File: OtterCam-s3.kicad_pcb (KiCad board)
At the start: 4 copper layers, 49.7 x 49.7 mm, 167 parts, among them J1 UART, J2 SD, J3 USB, J4 49F-1201GYD2NL, J5 MIPI, Q1 DTA114YKA, SW1 RST, U1 AllWinner-S3(FBGA-234), U2 AXP209(QFN-48), U3 SY8089AAAC, U4 AP6236, X1 26Mhz TCXO, Y1 32.768kHz, Y2 24MHz

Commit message: updated files
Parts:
- J3: footprint otter:USB-C 16Pin -> otter:918-418K2022Y40004
- J4: value 49F-1201GYD2NL -> RJ45_Shielded; footprint otter:49F-1201GYDXNL -> otter:1-338088-3
- moved J4 4.35 mm to (60.8, 68.9), turned to 0 degrees
- moved D5 3.96 mm to (56.0, 90.6)
- moved R19 3.96 mm to (58.5, 90.6)
- moved J3 1.97 mm to (55.9, 85.2)
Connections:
- J4 pad 1: EPHY_RX_P -> Net-(J4-Pad1)
- J4 pad 2: EPHY_RX_N -> Net-(J4-Pad2)
- J4 pad 3: Net-(C67-Pad2) -> Net-(J4-Pad3)
- J4 pad 6: Net-(C66-Pad2) -> Net-(J4-Pad6)
- J4 pad 7: EPHY_TX_P -> Net-(J4-Pad7)
- J4 pad 8: EPHY_TX_N -> Net-(J4-Pad8)
- J4 pad SH: Net-(C65-Pad1) -> GND
- R56 pad 2: Net-(J4-Pad10) -> Net-(R56-Pad2)
- R57 pad 2: Net-(J4-Pad12) -> Net-(R57-Pad2)

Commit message: added files
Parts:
- removed R35, R36, R37, R38: DNP, otter:R_0402
- removed R58, R59, R60, R61: 51, otter:R_0402
- removed X1: 26Mhz TCXO, otter:2016_SMD_CRYSTAL
- added C12: 100n, otter:C_0805, F.Cu at (72.0, 70.8)
- added C70: 18p, otter:C_0402, F.Cu at (93.1, 80.8)
- added D7: YEL, LED_SMD:LED_0603_1608Metric_Castellated, F.Cu at (64.5, 52.8)
- added D8: GRN, LED_SMD:LED_0603_1608Metric_Castellated, F.Cu at (64.5, 55.3)
- added R20: 75, otter:R_0402, F.Cu at (71.5, 72.7)
- added R26: 75, otter:R_0402, F.Cu at (71.5, 68.9)
- added Y3: 26MHz, otter:Oscillator_3225, F.Cu at (92.1, 78.4)
- AE1: footprint otter:KH-5220-A56 -> Connector_Coaxial:U.FL_Hirose_U.FL-R-SMT-1_Vertical
- C31, C33, C35, C37, C57, C60, H1, H2, H3, H4: moved to B.Cu
- C65: value 1n -> 100n
- C66, C67: footprint otter:C_0402 -> otter:C_0805
- C68: value 100n -> 1n; footprint otter:C_0402 -> otter:C_0805
- C69: value 100n -> 18p
- J4: value RJ45_Shielded -> RJ45
- moved C46 119.2 mm to (78.1, 91.6), turned to 270 degrees
- moved R34 112.8 mm to (83.2, 81.2)
- moved R46 110.1 mm to (79.5, 91.4), turned to 45 degrees
- moved R33 106.5 mm to (81.2, 80.6), turned to 270 degrees
- moved R41 102.9 mm to (82.1, 82.2), turned to 315 degrees
- moved R39 102.3 mm to (80.2, 84.2), turned to 315 degrees
- moved C41 101.3 mm to (95.0, 86.1), turned to 45 degrees
- moved C47 100.7 mm to (76.6, 83.3), turned to 45 degrees
- moved R40 100.5 mm to (79.7, 82.4), turned to 315 degrees
- moved R42 100.2 mm to (82.5, 80.3)
- moved R43 98.7 mm to (81.4, 82.8), turned to 315 degrees
- moved C45 91.8 mm to (76.1, 82.4), turned to 45 degrees
- moved C48 91.3 mm to (78.9, 90.2), turned to 315 degrees
- moved L5 90.8 mm to (77.4, 85.6), turned to 45 degrees
- moved C44 85.3 mm to (90.0, 81.0), turned to 45 degrees
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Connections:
- C65 pad 1: Net-(C65-Pad1) -> EPHY_RX_P
- C65 pad 2: GND -> Net-(C65-Pad2)
- C66 pad 1: GND -> EPHY_TX_P
- C67 pad 1: GND -> EPHY_TX_N
- C68 pad 1: GND -> Net-(C68-Pad1)
- C68 pad 2: Net-(C68-Pad2) -> GND
- C69 pad 1: GND -> Net-(C69-Pad1)
- C69 pad 2: Net-(C69-Pad2) -> GND
- J4 pad 1: Net-(J4-Pad1) -> Net-(C66-Pad2)
- J4 pad 2: Net-(J4-Pad2) -> Net-(C67-Pad2)
- J4 pad 3: Net-(J4-Pad3) -> Net-(C65-Pad2)
- J4 pad 5: Net-(J4-Pad5) -> Net-(J4-Pad4)
- J4 pad 8: Net-(J4-Pad8) -> Net-(J4-Pad7)
- U4 pad 11: Net-(U4-Pad11) -> Net-(C69-Pad1)
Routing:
- net VCC-DDR: track 0.00 -> 0.77 mm, vias 0 -> 1
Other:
- board size 49.7 x 49.7 mm -> 49.8 x 49.8 mm

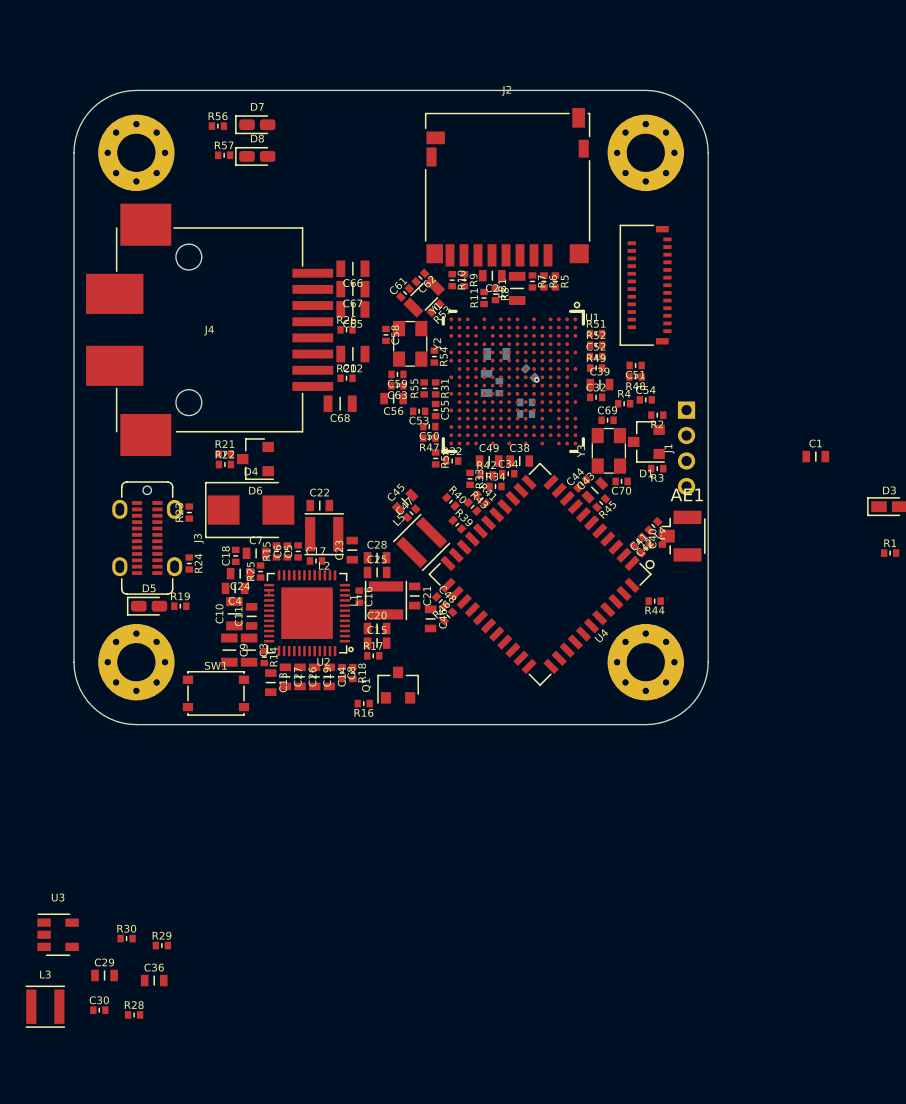
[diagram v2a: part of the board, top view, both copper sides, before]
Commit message: routed mipi, eth and sdio
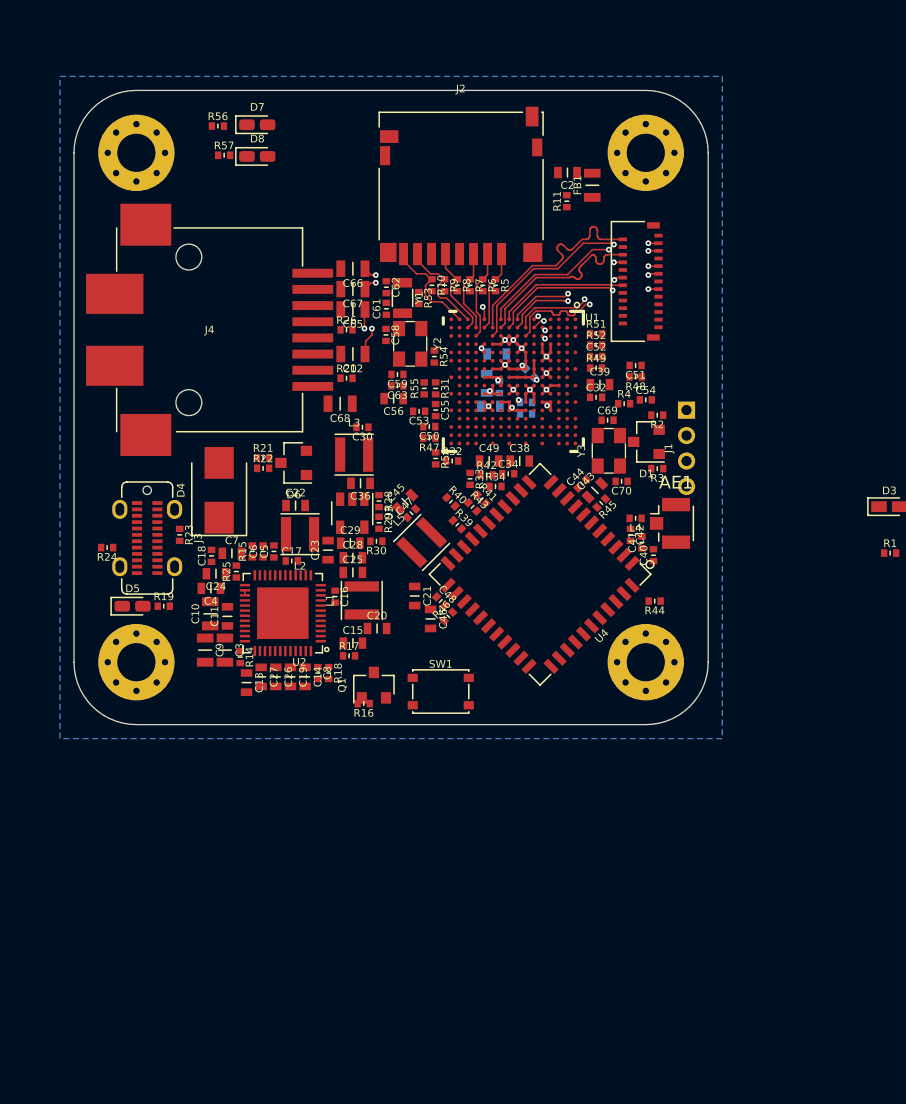
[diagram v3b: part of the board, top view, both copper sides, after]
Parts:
- C1: moved to B.Cu
- moved C30 50.2 mm to (72.8, 76.5), turned to 180 degrees
- moved L3 49.7 mm to (72.1, 78.7)
- moved R28 44.7 mm to (74.0, 82.3), turned to 270 degrees
- moved C36 42.3 mm to (72.6, 81.0), turned to 180 degrees
- moved U3 40.4 mm to (72.0, 83.3), turned to 270 degrees
- moved C29 39.1 mm to (71.8, 85.7)
- moved R29 37.3 mm to (74.0, 84.0), turned to 270 degrees
- moved R30 36.9 mm to (73.8, 85.5), turned to 180 degrees
- moved C1 25.9 mm to (82.8, 74.9)
- moved SW1 17.7 mm to (78.9, 97.3)
- moved C2 10.0 mm to (88.8, 56.5)
- moved FB1 10.0 mm to (90.8, 57.5)
- moved R11 10.0 mm to (88.8, 58.8)
- moved R24 6.57 mm to (52.7, 86.0), turned to 180 degrees
- moved R7 4.91 mm to (81.2, 65.4)
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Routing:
- net GND: track 0.00 -> 28.4 mm, vias 0 -> 12
- net EPHY_TX_P: track 0.00 -> 19.6 mm, vias 0 -> 2
- net EPHY_RX_P: track 0.00 -> 19.4 mm, vias 0 -> 2
- net EPHY_TX_N: track 0.00 -> 18.9 mm, vias 0 -> 2
- net EPHY_RX_N: track 0.00 -> 18.5 mm, vias 0 -> 2
- net MIPI_D3_P: track 0.00 -> 17.3 mm, vias 0 -> 2
- net MIPI_D3_N: track 0.00 -> 17.1 mm
- net MIPI_D2_N: track 0.00 -> 15.2 mm, vias 0 -> 2
- net MIPI_D2_P: track 0.00 -> 14.4 mm
- net MIPI_CK_P: track 0.00 -> 13.7 mm, vias 0 -> 2
- net MIPI_D1_P: track 0.00 -> 13.5 mm, vias 0 -> 2
- net MIPI_D1_N: track 0.00 -> 13.4 mm, vias 0 -> 2
- net MIPI_D0_N: track 0.00 -> 12.8 mm, vias 0 -> 2
- net MIPI_D0_P: track 0.00 -> 12.5 mm, vias 0 -> 2
- net MIPI_CK_N: track 0.00 -> 10.4 mm
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- added copper zone on B.Cu, net GND

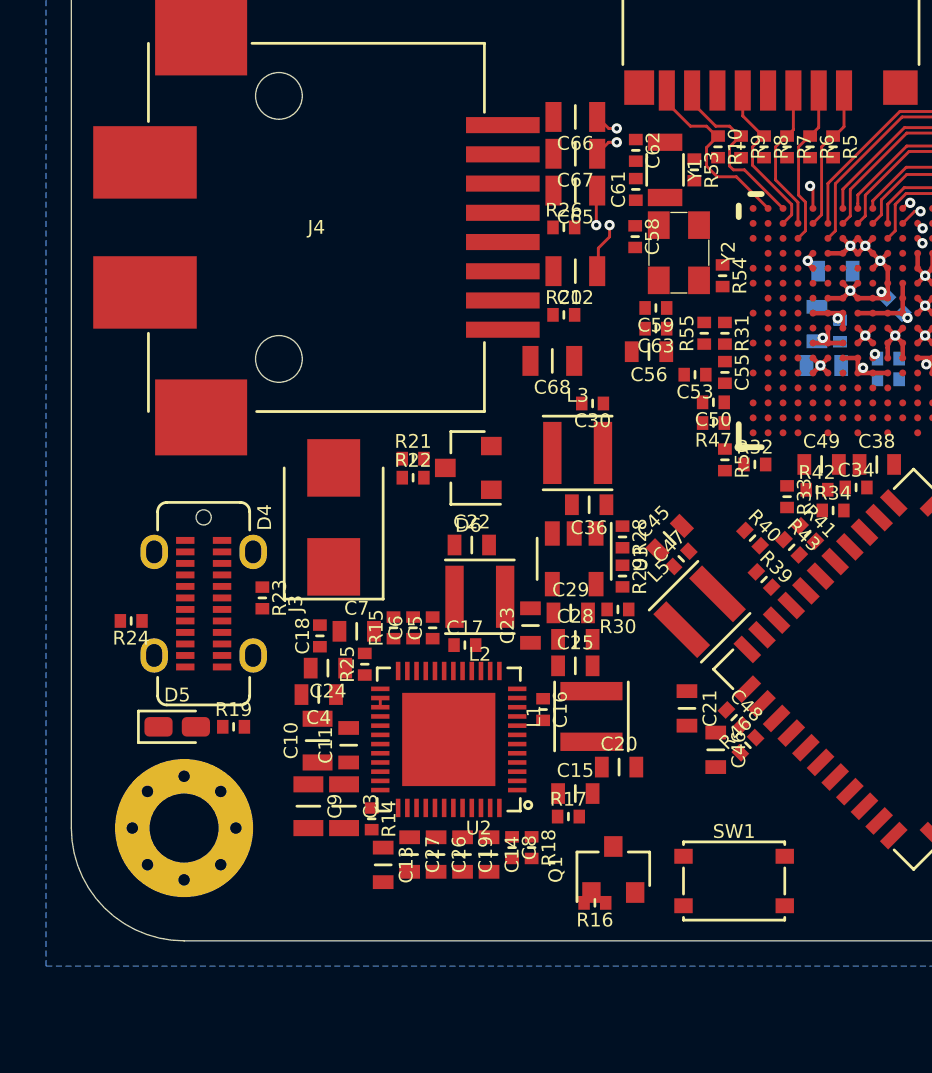
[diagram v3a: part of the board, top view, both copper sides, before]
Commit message: routed all high speed signals
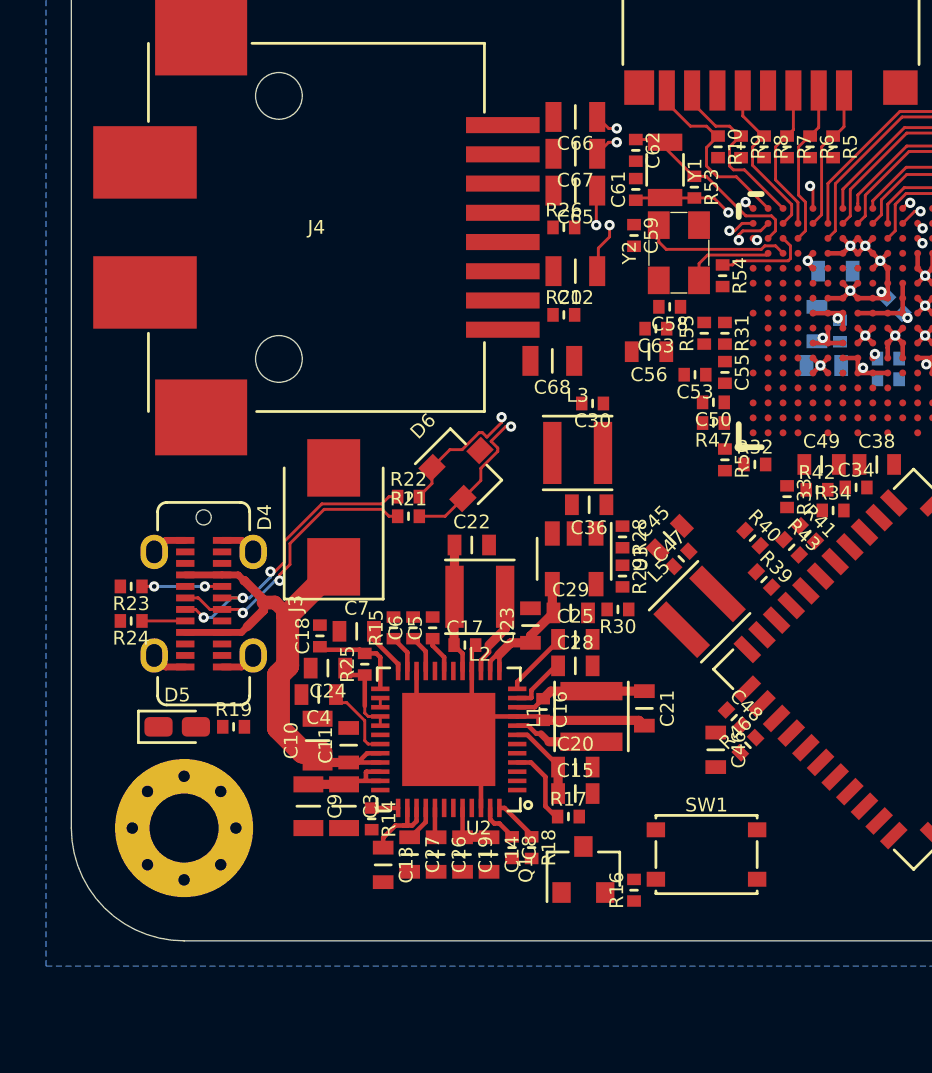
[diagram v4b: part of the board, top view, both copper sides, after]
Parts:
- moved R23 5.72 mm to (52.7, 84.5), turned to 180 degrees
- moved C58 3.40 mm to (76.1, 72.3), turned to 180 degrees
- moved C59 3.29 mm to (74.5, 69.2), turned to 270 degrees
- moved R21 2.51 mm to (64.8, 81.5)
- moved C20 1.90 mm to (72.0, 92.3)
- moved C21 1.85 mm to (75.0, 89.8)
- moved R16 1.79 mm to (74.5, 97.7), turned to 90 degrees
- moved SW1 1.66 mm to (77.7, 96.2)
- moved Q1 1.30 mm to (72.3, 96.8)
- moved C25 1.15 mm to (72.0, 86.8)
- moved C28 1.15 mm to (72.0, 88.0)
- moved R22 0.85 mm to (64.8, 80.6)
- moved R53 0.75 mm to (77.2, 67.2)
- moved D6 0.21 mm to (67.2, 79.3), turned to 45 degrees
- turned Y2 to 90 degrees
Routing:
- net GND: track 28.4 -> 54.4 mm, vias 12 -> 13
- net +5V: track 0.00 -> 23.9 mm
- net USB_D_N: track 0.00 -> 22.6 mm, vias 0 -> 2
- net USB_D_P: track 0.00 -> 21.2 mm, vias 0 -> 2
- net IPS: track 0.00 -> 20.8 mm
- net Net-(J3-PadA6): track 0.00 -> 13.1 mm, vias 0 -> 3
- net Net-(J3-PadA7): track 0.00 -> 12.2 mm, vias 0 -> 2
- net Net-(C62-Pad1): track 0.00 -> 8.60 mm
- net Net-(C59-Pad1): track 0.00 -> 6.46 mm
- net Net-(C61-Pad1): track 0.00 -> 6.27 mm, vias 0 -> 2
- net +1V1: track 5.19 -> 11.0 mm
- net +3V3: track 2.89 -> 8.53 mm
- net RESETn: track 0.00 -> 4.18 mm
- net AP_CK32KO: track 0.00 -> 4.07 mm
- net Net-(C58-Pad1): track 0.00 -> 3.91 mm
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
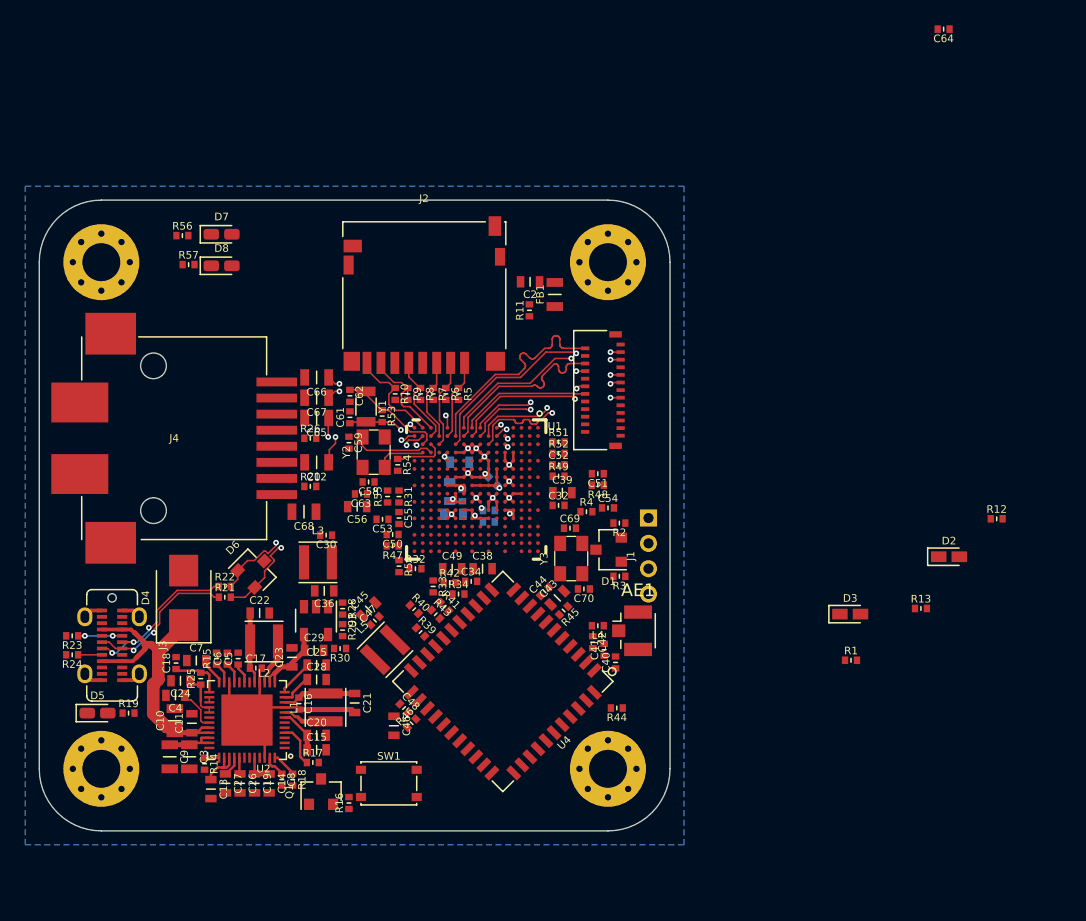
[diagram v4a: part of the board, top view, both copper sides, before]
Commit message: mostly routed
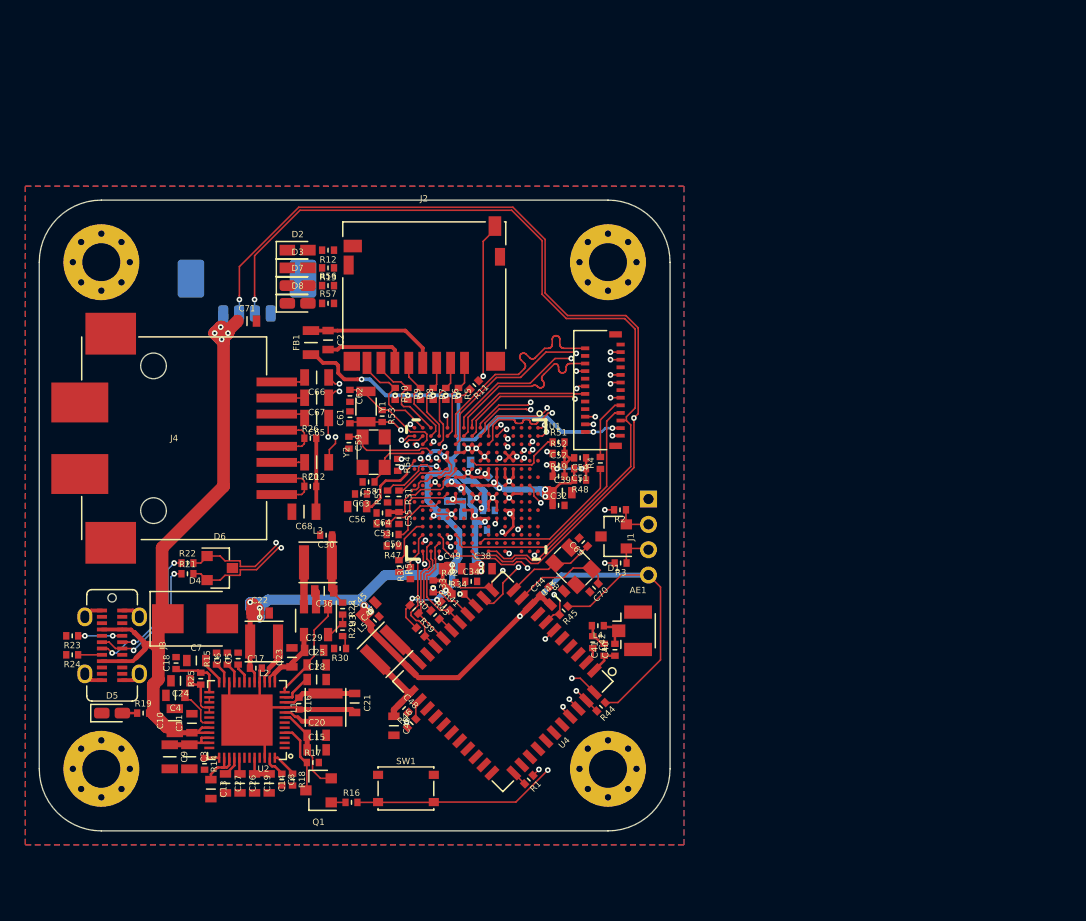
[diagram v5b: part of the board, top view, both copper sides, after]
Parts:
- added C71: 10u, otter:C_0603, F.Cu at (66.5, 59.6)
- added J6: LENS, Connector_Molex:Molex_PicoBlade_53398-0471_1x04-1MP_P1.25mm_Vertical, B.Cu at (66.5, 57.8)
- moved C64 58.5 mm to (77.2, 74.8)
- moved R12 56.9 mm to (72.9, 54.0), turned to 180 degrees
- moved D2 56.8 mm to (70.5, 54.0)
- moved R13 54.0 mm to (72.9, 55.5), turned to 180 degrees
- moved D3 51.5 mm to (70.5, 55.5)
- moved R1 27.1 mm to (88.8, 95.8), turned to 225 degrees
- moved FB1 19.6 mm to (71.5, 61.4)
- moved C2 16.6 mm to (72.9, 61.1), turned to 270 degrees
- moved R56 12.2 mm to (72.9, 56.9)
- moved R57 11.4 mm to (72.9, 58.2)
- moved R11 7.33 mm to (84.5, 64.7), turned to 225 degrees
- moved D7 7.25 mm to (70.5, 56.9)
- moved D8 6.70 mm to (70.5, 58.2)
- moved C54 4.52 mm to (92.8, 70.5), turned to 180 degrees
- moved R4 4.00 mm to (94.4, 70.8), turned to 90 degrees
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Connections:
- D7 pad 1: Net-(D7-Pad1) -> EPHY_SPD_LED
- D7 pad 2: +3V3 -> Net-(D7-Pad2)
- D8 pad 1: Net-(D8-Pad1) -> EPHY_LINK_LED
- D8 pad 2: +3V3 -> Net-(D8-Pad2)
- R56 pad 1: EPHY_SPD_LED -> Net-(D7-Pad2)
- R56 pad 2: Net-(D7-Pad1) -> +3V3
- R57 pad 1: EPHY_LINK_LED -> Net-(D8-Pad2)
- R57 pad 2: Net-(D8-Pad1) -> +3V3
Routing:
- net +3V3: track 8.53 -> 167.9 mm, vias 3 -> 25
- net MIPI_SDA: track 0.00 -> 75.1 mm, vias 0 -> 3
- net MIPI_SCK: track 0.00 -> 69.0 mm, vias 0 -> 1
- net GPIO_RST: track 0.00 -> 45.9 mm, vias 0 -> 2
- net +5V: track 23.9 -> 57.2 mm, vias 0 -> 4
- net GND: track 54.4 -> 79.4 mm, vias 13 -> 21
- net BT_UART_RX: track 0.00 -> 24.0 mm, vias 0 -> 2
- net BT_UART_RTS: track 0.00 -> 22.8 mm, vias 0 -> 2
- net BT_UART_TX: track 0.00 -> 22.2 mm, vias 0 -> 2
- net Net-(R1-Pad1): track 0.00 -> 22.2 mm, vias 0 -> 2
- net AP_CK32KO: track 4.07 -> 25.7 mm, vias 0 -> 3
- net MIPI_RESET: track 0.00 -> 21.1 mm
- net BT_UART_CTS: track 0.00 -> 18.8 mm, vias 0 -> 2
- net +1V1: track 11.0 -> 29.6 mm, vias 2 -> 7
- net VCC-DDR: track 4.31 -> 21.7 mm, vias 1 -> 5
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- added copper zone on F.Cu, net GND
- added copper zone on In2.Cu, net GND

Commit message: routing finished
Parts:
- added FID1: Fiducial, otter:FID_1.52, F.Cu at (60.0, 53.0)
- added FID2: Fiducial, otter:FID_1.52, F.Cu at (90.0, 97.0)
- moved C71 3.61 mm to (69.4, 61.8), turned to 90 degrees
- moved D2 0.70 mm to (70.5, 54.8)
- moved D8 0.70 mm to (70.5, 59.0)
- moved R12 0.70 mm to (72.9, 54.8)
- moved R57 0.70 mm to (72.9, 59.0)
- moved D3 0.70 mm to (70.5, 56.1)
- moved D7 0.70 mm to (70.5, 57.5)
- moved R13 0.70 mm to (72.9, 56.1)
- moved R56 0.70 mm to (72.9, 57.5)
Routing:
- net GPIO_LED2: track 0.00 -> 54.5 mm, vias 0 -> 2
- net GPIO_LED1: track 0.00 -> 51.6 mm, vias 0 -> 2
- net GND: track 79.4 -> 129.9 mm, vias 21 -> 183
- net IPS: track 24.3 -> 67.1 mm, vias 0 -> 11
- net +3.3V_RTC: track 7.27 -> 49.0 mm, vias 2 -> 5
- net MIPI_SCK: track 69.0 -> 102.0 mm, vias 1 -> 3
- net MIPI_SDA: track 75.1 -> 106.8 mm, vias 3 -> 5
- net EPHY_SPD_LED: track 0.00 -> 28.6 mm, vias 0 -> 2
- net EPHY_LINK_LED: track 0.00 -> 26.4 mm, vias 0 -> 2
- net RESETn: track 6.38 -> 32.3 mm, vias 0 -> 2
- net +1V1: track 29.6 -> 54.7 mm, vias 7 -> 10
- net VCC-DDR: track 21.7 -> 41.0 mm, vias 5 -> 7
- net +3.0VA: track 15.8 -> 29.4 mm, vias 0 -> 2
- net AP_CK32KO: track 25.7 -> 37.6 mm
- net +5V: track 57.2 -> 68.5 mm
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- added copper zone on In1.Cu, net GND
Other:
- outline, holes or cut-outs redrawn
- board text added: "@JanHenrikH 2021"
- board text added: "ACT"
- board text added: "Link"
- board text added: "OtterCam-s3"
- board text added: "Power"
- board text added: "Speed"
